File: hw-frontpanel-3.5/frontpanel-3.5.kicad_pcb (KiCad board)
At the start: 2 copper layers, 58.4 x 20.5 mm, 34 parts, among them J1 FRONT_PANEL, J2 QWIIC, J3 Conn_01x02_Pin, J5 OLED_SH1107, J6 Conn_01x12_MountingPin, SW1 SW_Push, SW2 SW_Push, SW3 SW_Push, SW4 SW_Push, U1 MT3540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

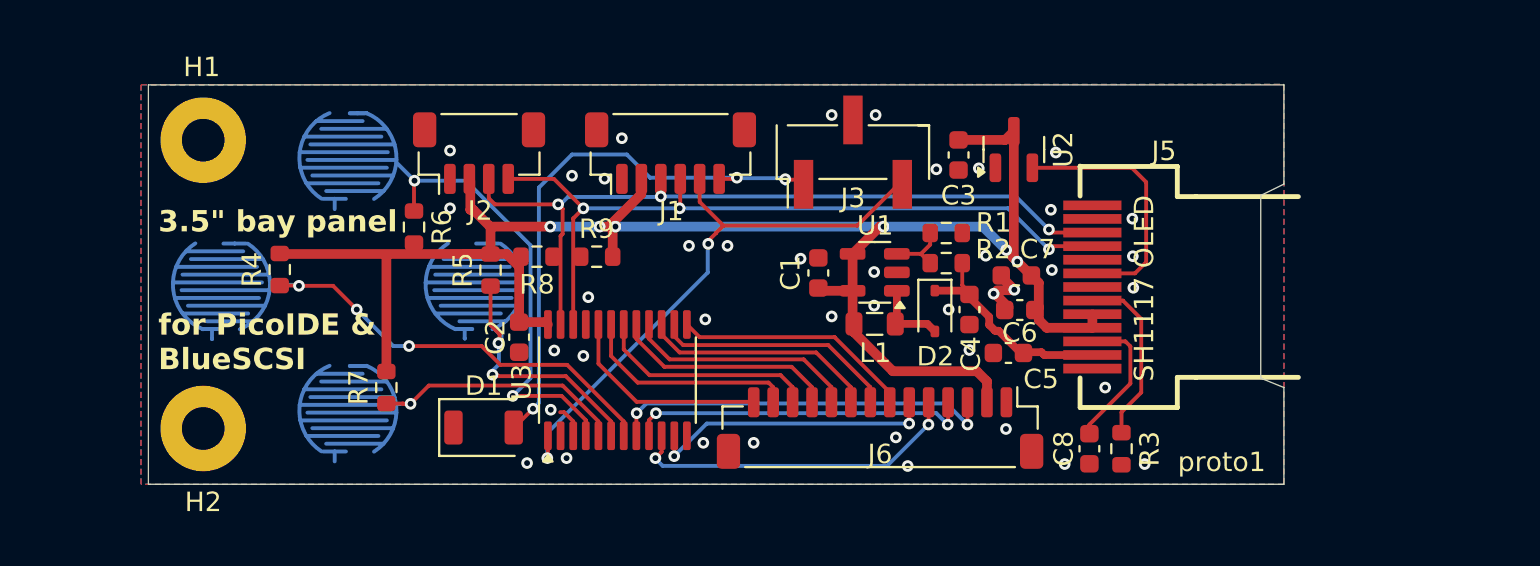
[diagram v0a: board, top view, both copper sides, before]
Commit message: Front panel board fabbed at JLCPCB 2025-09-17
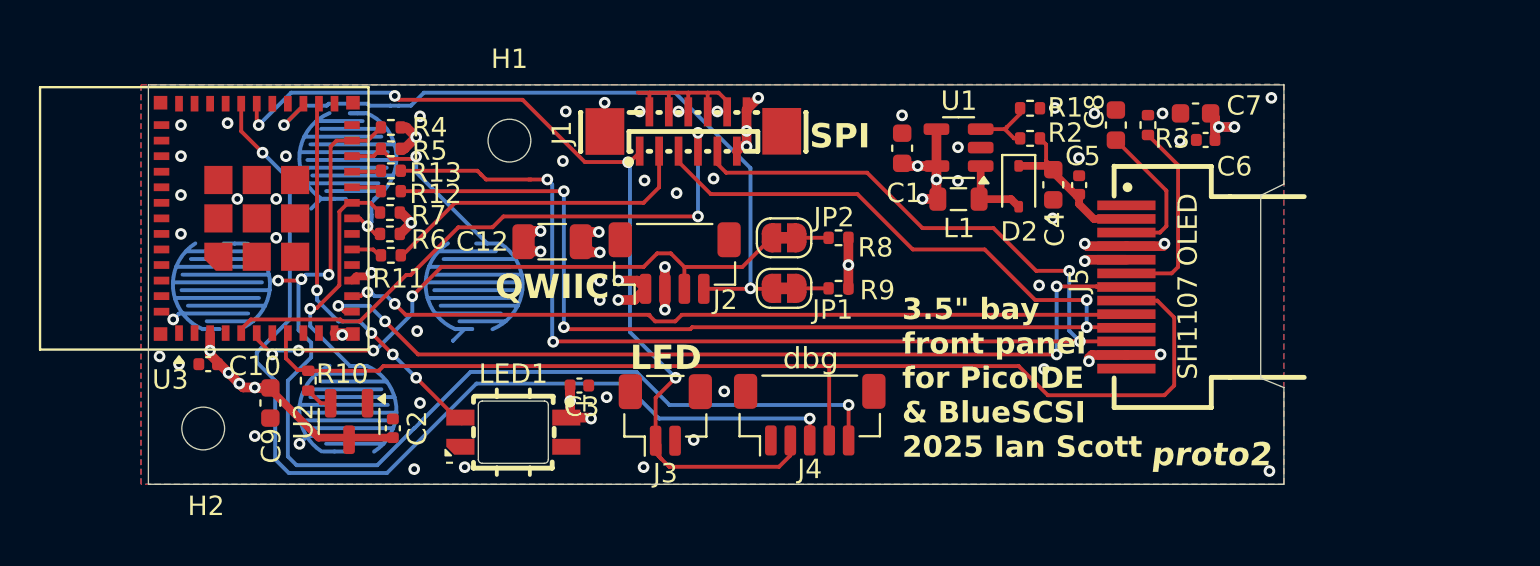
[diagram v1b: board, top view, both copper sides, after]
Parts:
- removed D1: LED, LED_SMD:LED_1206_3216Metric_ReverseMount_Hole1.8x2.4mm
- removed J6: Conn_01x12_MountingPin, Connector_JST:JST_SH_BM14B-SRSS-TB_1x14-1MP_P1.00mm_Vertical
- added C10: 1uF, Capacitor_SMD:C_0402_1005Metric, F.Cu at (138.0, 56.1)
- added C12: 100uF, Capacitor_SMD:C_1206_3216Metric, F.Cu at (155.7, 49.8)
- added C9: 10uF, Capacitor_SMD:C_0603_1608Metric, F.Cu at (141.2, 58.1)
- added J4: dbg, Connector_JST:JST_SH_BM05B-SRSS-TB_1x05-1MP_P1.00mm_Vertical, F.Cu at (168.9, 58.7)
- added JP1: SolderJumper_2_Bridged, Jumper:SolderJumper-2_P1.3mm_Bridged_RoundedPad1.0x1.5mm, F.Cu at (167.6, 52.2)
- added JP2: SolderJumper_2_Bridged, Jumper:SolderJumper-2_P1.3mm_Bridged_RoundedPad1.0x1.5mm, F.Cu at (167.6, 49.6)
- added LED1: SK6812MINI-E_C5149201, frontpanel:LED-SMD_L3.2-W2.8-LS5.9_SK6812MINI-E, F.Cu at (153.7, 59.6)
- added R10: 10K, Resistor_SMD:R_0402_1005Metric, F.Cu at (143.2, 57.0)
- added R11: 33, Resistor_SMD:R_0402_1005Metric, F.Cu at (147.4, 50.5)
- added R12: 33, Resistor_SMD:R_0402_1005Metric, F.Cu at (147.4, 47.2)
- added R13: 33, Resistor_SMD:R_0402_1005Metric, F.Cu at (147.4, 46.1)
- C2, C3, C5, C6: footprint Capacitor_SMD:C_0603_1608Metric -> Capacitor_SMD:C_0402_1005Metric
- H1, H2: footprint MountingHole:MountingHole_2.2mm_M2_Pad -> MountingHole:MountingHole_2.2mm_M2
- J1: value FRONT_PANEL -> SPI; footprint Connector_JST:JST_SH_BM06B-SRSS-TB_1x06-1MP_P1.00mm_Vertical -> frontpanel:FPC-SMD_12P-L11.5-W2.0-P0.50
- J3: value Conn_01x02_Pin -> LED; footprint Connector_PinHeader_2.54mm:PinHeader_1x03_P2.54mm_Vertical_SMD_Pin1Left -> Connector_JST:JST_SH_BM02B-SRSS-TB_1x02-1MP_P1.00mm_Vertical
- R1, R2, R3, R4, R5, R6, R7, R8, R9: footprint Resistor_SMD:R_0603_1608Metric -> Resistor_SMD:R_0402_1005Metric
- U3: value TCA9535PWR -> ESP32-C3-MINI-1; footprint Package_SO:TSSOP-24_4.4x7.8mm_P0.65mm -> RF_Module:ESP32-C6-MINI-1
- moved U2 37.0 mm to (145.2, 59.0), turned to -90 degrees
- moved C3 22.8 mm to (157.1, 57.2), turned to 0 degrees
- moved U3 20.3 mm to (140.5, 48.6)
- moved C8 16.7 mm to (184.7, 43.8), turned to -90 degrees
- moved R3 16.7 mm to (186.4, 43.8), turned to -90 degrees
- moved J3 16.6 mm to (161.5, 58.7), turned to 0 degrees
- moved H1 15.8 mm to (153.5, 44.6)
- moved R8 15.5 mm to (170.4, 49.6), turned to 0 degrees
- moved C6 13.0 mm to (189.3, 44.6)
- moved R9 12.5 mm to (170.4, 52.2)
- moved C7 12.4 mm to (188.8, 43.2)
- moved J2 11.5 mm to (162.0, 50.9)
- moved C5 9.37 mm to (182.8, 46.9), turned to 90 degrees
- moved R4 9.28 mm to (147.4, 43.9), turned to 0 degrees
- moved R7 9.00 mm to (147.3, 48.3), turned to 0 degrees
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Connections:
- J1 pad 1: GND -> /ACT_LED_IN/UART_RX
- J1 pad 2: +3V3 -> GND
- J1 pad 3: /SDA -> /HOST_CS
- J1 pad 4: /SCL -> GND
- J1 pad 5: /~{INT} -> /SPI_CLK
- J1 pad 6: /ACT_LED -> GND
- J3 pad 1: /ACT_LED -> /ACT_LED_IN/UART_RX
- J5 pad 10: /SCL -> /SPI_CLK
- J5 pad 11: /SDA -> /SPI_TX
- J5 pad 5: +3V3 -> GND
- J5 pad 7: GND -> /OLED_CS
- J5 pad 8: /~{RESET} -> /ESP32_EN
- J5 pad 9: GND -> /OLED_DC
- R8 pad 1: /SDA -> Net-(JP2-B)
- R9 pad 1: /SCL -> Net-(JP1-B)
- U3 pad 1: /~{INT} -> GND
- U3 pad 10: Net-(J6-Pin_5) -> unconnected-(U3-NC-Pad10)
- U3 pad 11: Net-(J6-Pin_6) -> GND
- U3 pad 12: GND -> /OLED_CS
- U3 pad 13: Net-(J6-Pin_7) -> /OLED_DC
- U3 pad 14: Net-(J6-Pin_8) -> GND
- U3 pad 15: Net-(J6-Pin_9) -> unconnected-(U3-NC-Pad15)
- U3 pad 17: Net-(J6-Pin_11) -> unconnected-(U3-NC-Pad17)
- U3 pad 18: Net-(J6-Pin_12) -> /P0_0
- U3 pad 19: Net-(J6-Pin_13) -> /P0_1
- U3 pad 21: GND -> Net-(U3-IO7)
- U3 pad 22: /SCL -> /P0_2
- U3 pad 23: /SDA -> /P0_3
- U3 pad 24: +3V3 -> unconnected-(U3-NC-Pad24)
- U3 pad 3: GND -> +3V3
- U3 pad 4: /P0_0 -> unconnected-(U3-NC-Pad4)
- U3 pad 5: /P0_1 -> /SPI_RX
- U3 pad 6: /P0_2 -> /SDA
- U3 pad 7: /P0_3 -> unconnected-(U3-NC-Pad7)
- U3 pad 8: Net-(J6-Pin_3) -> /ESP32_EN
- U3 pad 9: Net-(J6-Pin_4) -> unconnected-(U3-NC-Pad9)
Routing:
- net /SPI_TX: track 0.00 -> 70.6 mm, vias 0 -> 4
- net /SPI_CLK: track 0.00 -> 70.3 mm, vias 0 -> 4
- net /ESP32_EN: track 0.00 -> 58.4 mm
- net +3V3: track 96.3 -> 42.8 mm, vias 6 -> 23
- net /UART_TX: track 0.00 -> 52.2 mm, vias 0 -> 2
- net /ACT_LED_IN/UART_RX: track 0.00 -> 48.3 mm, vias 0 -> 4
- net /OLED_CS: track 0.00 -> 45.9 mm, vias 0 -> 4
- net /OLED_DC: track 0.00 -> 40.7 mm, vias 0 -> 2
- net /P0_3: track 22.7 -> 56.6 mm, vias 3 -> 4
- net /SPI_RX: track 0.00 -> 31.4 mm, vias 0 -> 2
- net /~{INT}: track 30.0 -> 0.00 mm, vias 2 -> 0
- net /ACT_LED: track 29.1 -> 0.00 mm, vias 3 -> 0
- net /LED_DATA: track 0.00 -> 20.8 mm, vias 0 -> 4
- net Net-(J6-Pin_3): track 20.0 -> 0.00 mm, vias 2 -> 0
- net GND: track 6.91 -> 26.7 mm, vias 41 -> 56
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- added copper zone on In2.Cu, net +3V3
- added copper zone on In1.Cu, net GND
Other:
- copper layers 2 -> 4
- board text added: "3.5{dblquote} bay front panel for PicoIDE & BlueSCSI 2025 Ian Scott"
- board text added: "LED"
- board text added: "QWIIC"
- board text added: "SH1107 OLED"
- board text added: "SPI"
- board text added: "dbg"
- board text added: "proto2"
- board text removed: "3.5{dblquote} bay panel for PicoIDE & BlueSCSI"
- board text removed: "SH1117 OLED"
- board text removed: "proto1"

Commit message: Use RC for ESP32 reset, power on reset for OLED
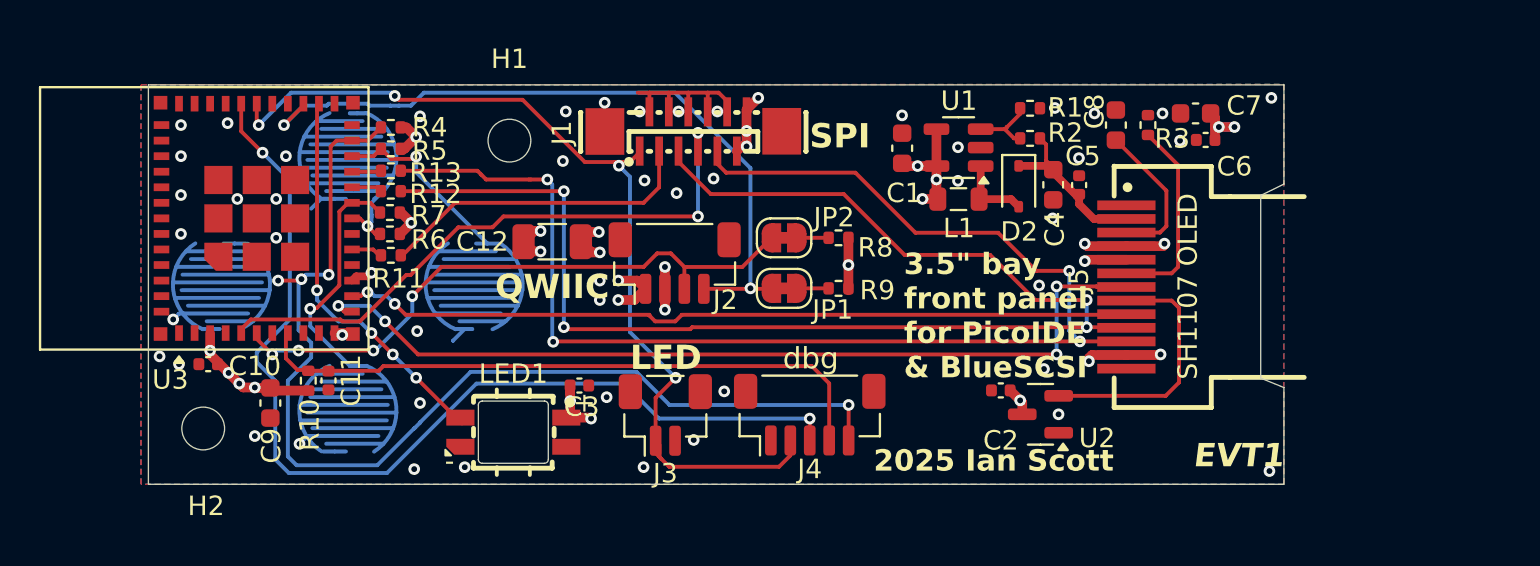
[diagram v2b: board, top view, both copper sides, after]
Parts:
- added C11: 1uF, Capacitor_SMD:C_0402_1005Metric, F.Cu at (144.2, 56.9)
- moved U2 35.6 mm to (180.8, 58.7), turned to 180 degrees
- moved C2 31.3 mm to (178.8, 57.5), turned to 180 degrees
- turned R10 to -90 degrees
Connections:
- J5 pad 8: /ESP32_EN -> /~{RESET}
- R10 pad 1: /~{RESET} -> /ESP32_EN
- R10 pad 2: /ESP32_EN -> +3V3
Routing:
- net /ESP32_EN: track 58.4 -> 33.0 mm
- net /~{RESET}: track 1.42 -> 13.2 mm
- net +3V3: track 42.8 -> 38.9 mm, vias 23 -> 24
- net GND: vias 56 -> 57
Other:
- board text added: "2025 Ian Scott"
- board text added: "3.5{dblquote} bay front panel for PicoIDE & BlueSCSI"
- board text added: "EVT1"
- board text removed: "3.5{dblquote} bay front panel for PicoIDE & BlueSCSI 2025 Ian Scott"
- board text removed: "proto2"

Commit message: Provisional v1.0.0 hardware
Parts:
- J4: value dbg -> TC2030; footprint Connector_JST:JST_SH_BM05B-SRSS-TB_1x05-1MP_P1.00mm_Vertical -> Connector:Tag-Connect_TC2030-IDC-NL_2x03_P1.27mm_Vertical
- moved J4 20.2 mm to (148.7, 58.8), turned to -90 degrees
- moved C3 3.29 mm to (158.2, 60.3), turned to -90 degrees
- moved C9 2.27 mm to (139.9, 56.2), turned to 0 degrees
- moved R10 0.84 mm to (142.4, 56.6), turned to 180 degrees
- moved C10 0.67 mm to (137.4, 56.4)
- moved C11 0.33 mm to (144.3, 56.6), turned to 0 degrees
- moved LED1 0.30 mm to (154.0, 59.6)
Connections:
- J4 pad 1: GND -> /ESP32_EN
- J4 pad 2: /ACT_LED_IN/UART_RX -> +3V3
- J4 pad 4: /ESP32_EN -> GND
- J4 pad 5: /P0_3 -> /ACT_LED_IN/UART_RX
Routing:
- net /UART_TX: track 52.2 -> 24.5 mm
- net /ESP32_EN: track 33.0 -> 8.05 mm
- net /P0_3: track 56.6 -> 31.9 mm
- net /ACT_LED_IN/UART_RX: track 48.5 -> 54.9 mm, vias 4 -> 7
- net +3V3: track 38.9 -> 45.0 mm
- net GND: track 26.7 -> 29.7 mm, vias 57 -> 56
- net /LED_DATA: track 20.8 -> 23.3 mm
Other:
- board text added: "LED IN"
- board text added: "v1.0.0"
- board text added: "x01"
- board text added: "© 2025 Ian Scott - CERN-OHL-P v2"
- board text removed: "2025 Ian Scott"
- board text removed: "EVT1"
- board text removed: "LED"

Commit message: Final candidate v1.0.0 hardware
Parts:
- moved C10 0.32 mm to (137.4, 56.1)
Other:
- board text added: "x02"
- board text removed: "x01"

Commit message: Final v1.0.0 front panel design
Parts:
- added J6: dbg, Connector_JST:JST_SH_BM05B-SRSS-TB_1x05-1MP_P1.00mm_Vertical, F.Cu at (163.0, 58.7)
- moved J3 9.91 mm to (171.4, 58.5)
- moved C11 0.63 mm to (143.9, 57.1), turned to -90 degrees
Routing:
- net /UART_TX: track 24.5 -> 60.5 mm, vias 2 -> 3
- net /ESP32_EN: track 8.05 -> 30.3 mm, vias 0 -> 2
- net /P0_3: track 31.9 -> 50.6 mm, vias 4 -> 5
- net /ACT_LED_IN/UART_RX: track 54.9 -> 66.4 mm
- net +3V3: track 45.0 -> 39.4 mm, vias 24 -> 25
- net GND: track 29.7 -> 31.4 mm, vias 56 -> 63
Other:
- board text added: "ACT"
- board text added: "f01"
- board text added: "open retro storage 3.5{dblquote} bay front panel"
- board text added: "prog"
- board text added: "© 2025 Ian Scott - CERN-OHL-S v2"
- board text removed: "3.5{dblquote} bay front panel for PicoIDE & BlueSCSI"
- board text removed: "LED IN"
- board text removed: "QWIIC"
- board text removed: "x02"
- board text removed: "© 2025 Ian Scott - CERN-OHL-P v2"
